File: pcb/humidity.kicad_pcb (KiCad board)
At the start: 2 copper layers, 59.7 x 27.9 mm, 15 parts, among them J1 Battery Holder, J2 Conn_01x06, Q1 Q_NMOS_GSD, U1 BME280, U2 ESP32-WROOM-32

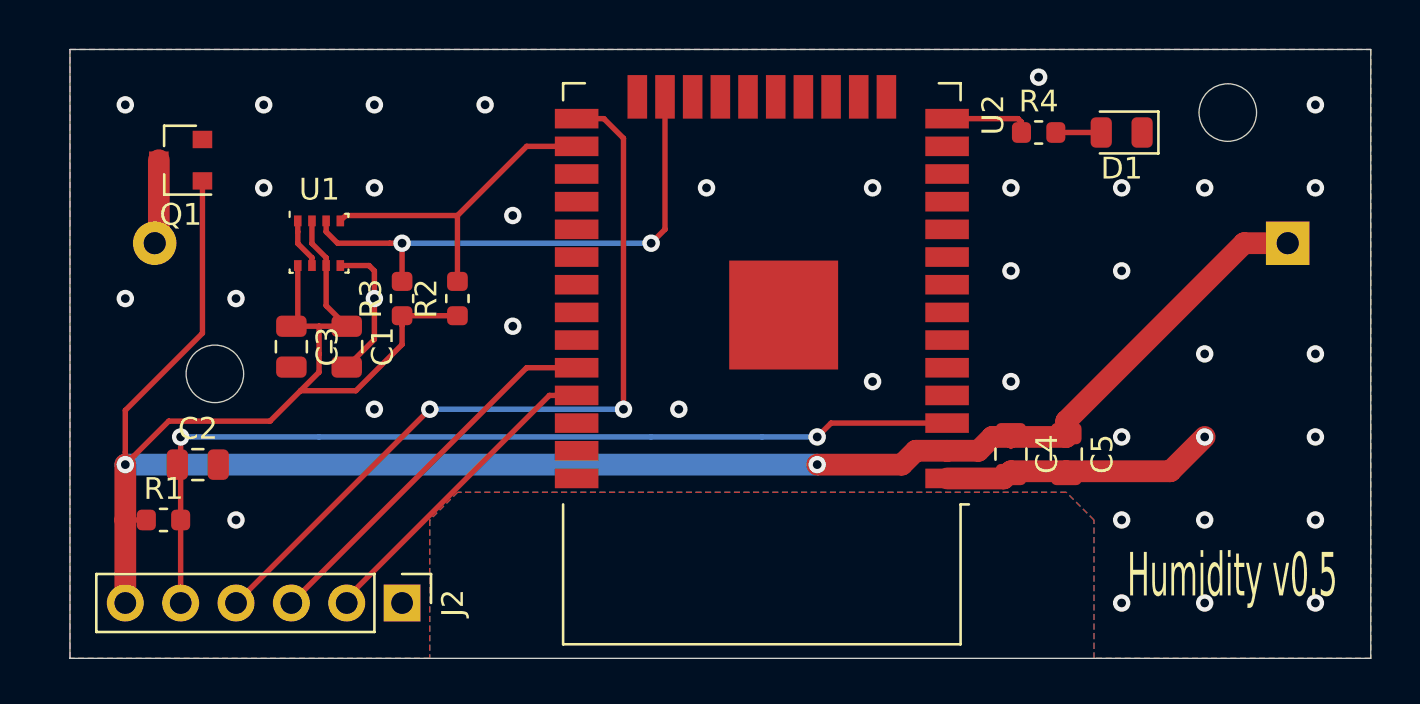
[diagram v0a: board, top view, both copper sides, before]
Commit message: pcb: Update pcb with new routing (pcb v0.6)
Move esp32 chip to side of board to allow more space for other
components.

Move bme280 chip away from battery and do not extend the ground plane
under it.  This is intended to improve thermal isolation of the bme280
chip.

Route most unused micro-controller pins to 2.54mm pins that are
externally accessible.

Add a surface mounted button component to the board.

Remove reverse battery diode.  The physical battery holder should
prevent the battery from being inserted in an incorrect orientation.

Note PCB revision on silkscreen as "v0.6".

Signed-off-by: Kevin O'Connor <kevin@koconnor.net>
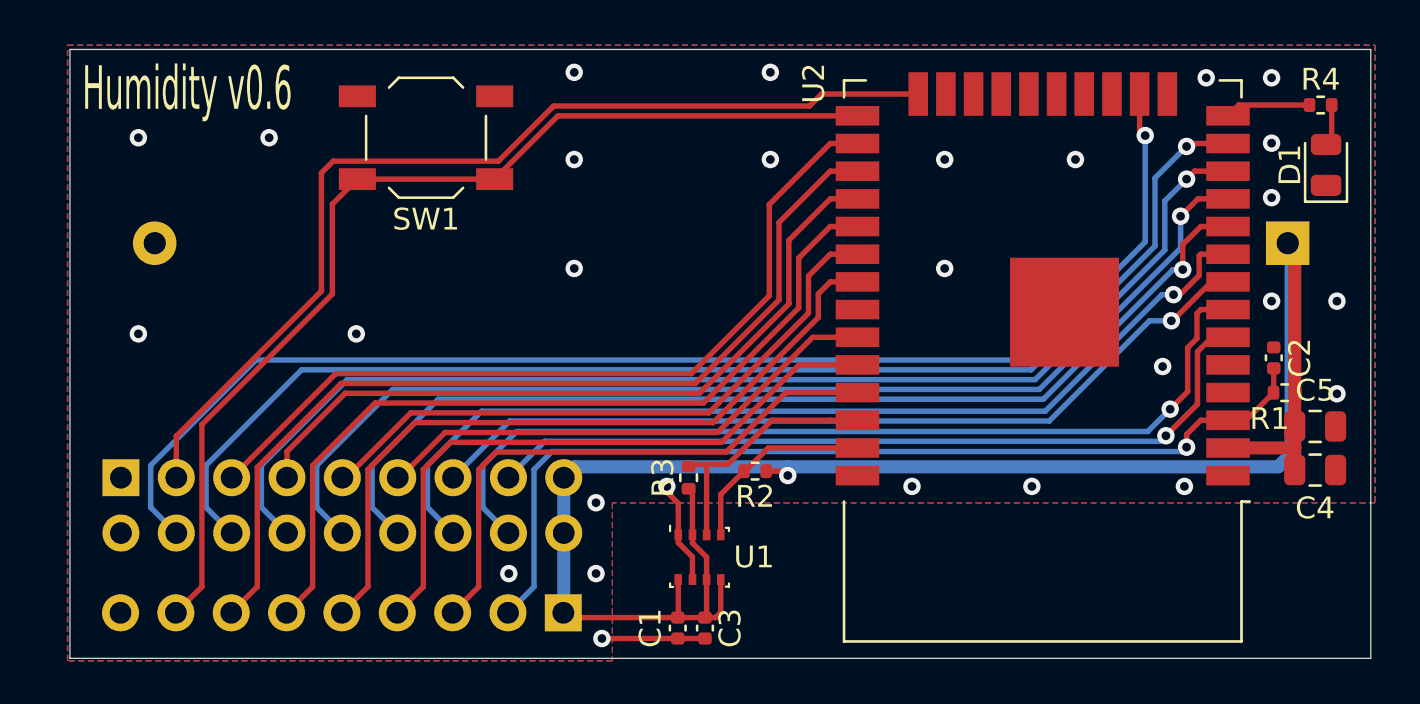
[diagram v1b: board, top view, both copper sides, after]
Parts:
- removed Q1: Q_NMOS_GSD, Package_TO_SOT_SMD:SOT-23
- added J3: Conn_02x09_Odd_Even, Connector_PinHeader_2.54mm:PinHeader_2x09_P2.54mm_Vertical, B.Cu at (152.2, 127.6)
- added SW1: SW_Push, Button_Switch_SMD:SW_SPST_TL3342, F.Cu at (166.2, 112.0)
- C1, C2, C3: footprint Capacitor_SMD:C_0805_2012Metric -> Capacitor_SMD:C_0402_1005Metric
- J2: value Conn_01x06 -> Conn_01x09; footprint Connector_PinHeader_2.54mm:PinHeader_1x06_P2.54mm_Vertical -> Connector_PinHeader_2.54mm:PinHeader_1x09_P2.54mm_Vertical; moved to B.Cu
- R1, R2, R3, R4: footprint Resistor_SMD:R_0603_1608Metric -> Resistor_SMD:R_0402_1005Metric
- moved R1 51.8 mm to (205.6, 123.7), turned to 180 degrees
- moved C2 49.6 mm to (205.1, 122.1), turned to 90 degrees
- moved C3 23.0 mm to (179.0, 134.5)
- moved U1 22.6 mm to (178.8, 131.2)
- moved C1 19.9 mm to (177.8, 134.5)
- moved R2 15.8 mm to (181.3, 127.3), turned to 180 degrees
- moved R3 15.5 mm to (178.2, 127.6)
- moved C4 14.0 mm to (207.0, 127.2), turned to 0 degrees
- moved R4 13.0 mm to (207.2, 110.5)
- moved U2 12.9 mm to (194.5, 119.2)
- moved C5 11.5 mm to (207.0, 125.2), turned to 0 degrees
- moved D1 9.50 mm to (207.5, 113.2), turned to 90 degrees
- moved J2 7.41 mm to (172.5, 133.8), turned to 90 degrees
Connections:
- J1 pad 2: Net-(J1-Pad2) -> GND
- J2 pad 1: GND -> +BATT
- J2 pad 2: TXD -> RESET
- J2 pad 3: RXD -> TXD
- J2 pad 4: BOOT -> RXD
- J2 pad 5: RESET -> IO19
- J2 pad 6: +BATT -> IO5
- U1 pad 5: GND -> +BATT
- U2 pad 10: Net-(U2-Pad10) -> IO25
- U2 pad 11: Net-(U2-Pad11) -> IO26
- U2 pad 12: Net-(U2-Pad12) -> IO27
- U2 pad 13: Net-(U2-Pad13) -> IO14
- U2 pad 16: Net-(U2-Pad16) -> IO13
- U2 pad 23: SDA -> Net-(U2-Pad23)
- U2 pad 24: Net-(U2-Pad24) -> IO2
- U2 pad 26: SCL -> IO4
- U2 pad 27: Net-(U2-Pad27) -> IO16
- U2 pad 28: Net-(U2-Pad28) -> IO17
- U2 pad 29: Net-(U2-Pad29) -> IO5
- U2 pad 30: Net-(U2-Pad30) -> IO18
- U2 pad 31: Net-(U2-Pad31) -> IO19
- U2 pad 33: Net-(U2-Pad33) -> IO21
- U2 pad 36: Net-(U2-Pad36) -> SDA
- U2 pad 37: Net-(U2-Pad37) -> SCL
- U2 pad 6: Net-(U2-Pad6) -> IO34
- U2 pad 7: Net-(U2-Pad7) -> IO35
- U2 pad 8: Net-(U2-Pad8) -> IO32
- U2 pad 9: Net-(U2-Pad9) -> IO33
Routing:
- net IO13: track 0.00 -> 60.4 mm, vias 0 -> 1
- net IO14: track 0.00 -> 58.4 mm, vias 0 -> 1
- net IO27: track 0.00 -> 54.9 mm, vias 0 -> 1
- net IO26: track 0.00 -> 51.3 mm, vias 0 -> 1
- net IO25: track 0.00 -> 48.1 mm, vias 0 -> 1
- net IO2: track 0.00 -> 45.8 mm
- net IO33: track 0.00 -> 45.6 mm, vias 0 -> 1
- net IO35: track 0.00 -> 42.8 mm, vias 0 -> 1
- net IO16: track 0.00 -> 42.4 mm
- net IO32: track 0.00 -> 39.3 mm, vias 0 -> 1
- net IO5: track 0.00 -> 38.1 mm
- net IO34: track 0.00 -> 37.9 mm, vias 0 -> 1
- net IO4: track 0.00 -> 37.5 mm
- net IO17: track 0.00 -> 33.9 mm
- net IO19: track 0.00 -> 33.7 mm
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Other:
- net class Tiny added: clearance 0.127, trace_width 0.127, via_dia 0.6, via_drill 0.3
- rule trace_min: 0.2 -> 0.05
- rule via_min_size: 0.4 -> 0.6
- board text added: "3V"
- board text added: "BOOT"
- board text added: "GND"
- board text added: "Humidity v0.6"
- board text added: "IO13"
- board text added: "IO14"
- board text added: "IO16"
- board text added: "IO17"
- board text added: "IO18"
- board text added: "IO19"
- board text added: "IO2"
- board text added: "IO21"
- board text added: "IO25"
- board text added: "IO26"
- board text added: "IO27"
- board text added: "IO32"
- board text added: "IO33"
- board text added: "IO34"
- board text added: "IO35"
- board text added: "IO4"
- board text added: "IO5"
- board text added: "RESET"
- board text added: "Rx"
- board text added: "Tx"
- board text removed: "Humidity v0.5"

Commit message: pcb: Update to use SHT-31 humidity chip
Replace bme280 with sht31 humidity chip.

Add jlcpcb tooling holes to the board.

Save gerber files to pcb/out/ directory.

Signed-off-by: Kevin O'Connor <kevin@koconnor.net>
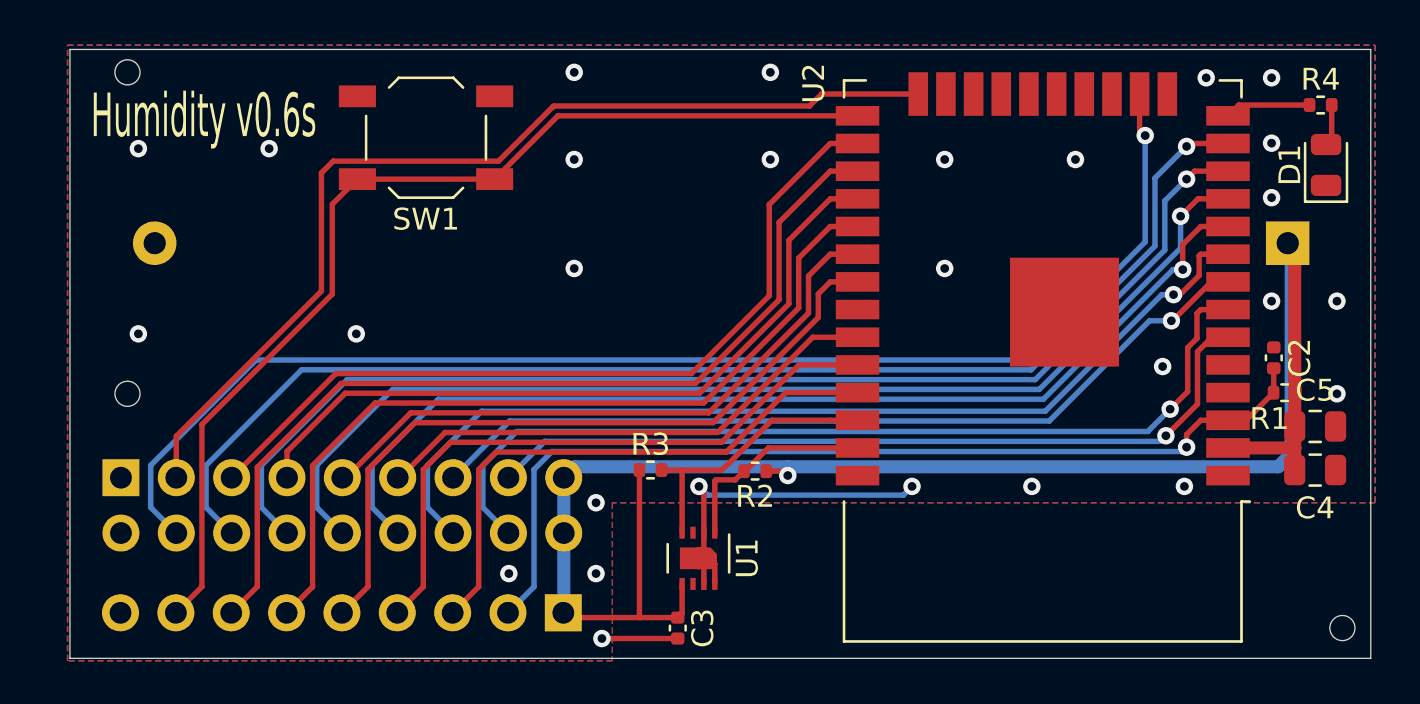
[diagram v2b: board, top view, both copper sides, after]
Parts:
- removed C1: 100nF, Capacitor_SMD:C_0402_1005Metric
- added REF**: tooling_hole, pcb:tooling_hole, F.Cu at (208.2, 134.5)
- added REF**: tooling_hole, pcb:tooling_hole, F.Cu at (152.5, 123.8)
- added REF**: tooling_hole, pcb:tooling_hole, F.Cu at (152.5, 109.0)
- R1: value 10K -> 10K Ohm
- R2, R3: value 4K7 -> 4.7K Ohm
- R4: value 0K1 -> 100 Ohm
- U1: value BME280 -> SHT31-DIS; footprint Package_LGA:Bosch_LGA-8_2.5x2.5mm_P0.65mm_ClockwisePinNumbering -> Sensor_Humidity:Sensirion_DFN-8-1EP_2.5x2.5mm_P0.5mm_EP1.1x1.7mm
- moved R3 1.78 mm to (176.5, 127.2), turned to 0 degrees
- moved C3 1.25 mm to (177.8, 134.5)
- moved U1 0.07 mm to (178.7, 131.3), turned to 270 degrees
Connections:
- R2 pad 2: SCL -> SDA
- R3 pad 2: SDA -> SCL
- U1 pad 1: GND -> SDA
- U1 pad 2: +BATT -> GND
- U1 pad 3: SDA -> Net-(U1-Pad3)
- U1 pad 6: +BATT -> Net-(U1-Pad6)
- U1 pad 8: +BATT -> GND
- U2 pad 36: SDA -> SCL
- U2 pad 37: SCL -> SDA
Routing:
- net GND: track 9.85 -> 20.5 mm
- net SCL: track 9.02 -> 12.8 mm
- net +BATT: track 82.2 -> 78.9 mm
- net SDA: track 11.9 -> 9.55 mm
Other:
- board text added: "Humidity v0.6s"
- board text removed: "Humidity v0.6"
